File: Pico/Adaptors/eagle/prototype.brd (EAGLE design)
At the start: 45.8 x 20.7 mm, 13 parts, among them J1 JST-2P-SMD-PW-3410050P1

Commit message: minor board tweaks
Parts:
- flipped J1 to the bottom, turned to 90 degrees
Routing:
- net N$15: track 13.4 -> 20.2 mm
- net GND: track 20.2 -> 23.1 mm, vias 3 -> 2
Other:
- board text added: "Pico This Side"
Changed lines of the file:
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@@
 <wire x1="45.771" y1="20.437" x2="0" y2="20.564" width="0" layer="20"/>
 <wire x1="0" y1="20.564" x2="0" y2="0" width="0" layer="20"/>
+<text x="10.795" y="7.366" size="0.8128" layer="25">Pico This Side</text>
 </plain>
 <attributes>
@@
 <attribute name="VALUE" x="41.275" y="20.32" size="1.27" layer="27" rot="R270"/>
 </element>
-<element name="J1" library="OPL Eagle Library" package="2P-SMD-2.0-90D" value="JST-2P-SMD-PW-3410050P1" x="3.81" y="10.16" smashed="yes" rot="R270"/>
+<element name="J1" library="OPL Eagle Library" package="2P-SMD-2.0-90D" value="JST-2P-SMD-PW-3410050P1" x="3.81" y="10.16" smashed="yes" rot="MR90"/>
 </elements>
 <signals>
@@
 <contactref element="J1" pad="3"/>
 <contactref element="J1" pad="4"/>
-<wire x1="8.89" y1="9.16" x2="1.762" y2="9.16" width="0.6096" layer="1"/>
-<wire x1="1.762" y1="9.16" x2="1.651" y2="9.271" width="0.6096" layer="1"/>
-<wire x1="1.651" y1="9.271" x2="1.651" y2="14.038" width="0.6096" layer="1"/>
-<wire x1="1.651" y1="14.038" x2="1.629" y2="14.06" width="0.6096" layer="1"/>
-<wire x1="1.762" y1="9.16" x2="1.762" y2="6.393" width="0.6096" layer="1"/>
-<wire x1="1.762" y1="6.393" x2="1.629" y2="6.26" width="0.6096" layer="1"/>
-<wire x1="1.629" y1="6.26" x2="1.629" y2="4.169" width="0.6096" layer="1"/>
-<wire x1="1.629" y1="4.169" x2="1.27" y2="3.81" width="0.6096" layer="1"/>
-<via x="1.778" y="9.144" extent="1-16" drill="0.3048"/>
 <via x="19.558" y="14.224" extent="1-16" drill="0.3048"/>
 <via x="19.558" y="6.604" extent="1-16" drill="0.3048"/>
+<wire x1="1.27" y1="3.81" x2="1.27" y2="5.901" width="0.6096" layer="16"/>
+<wire x1="1.27" y1="5.901" x2="1.629" y2="6.26" width="0.6096" layer="16"/>
+<wire x1="1.629" y1="6.26" x2="1.629" y2="14.06" width="0.6096" layer="16"/>
+<wire x1="1.629" y1="14.06" x2="1.629" y2="11.198" width="0.6096" layer="16"/>
+<wire x1="1.629" y1="11.198" x2="1.651" y2="11.176" width="0.6096" layer="16"/>
+<wire x1="1.651" y1="11.176" x2="8.874" y2="11.176" width="0.6096" layer="16"/>
+<wire x1="8.874" y1="11.176" x2="8.89" y2="11.16" width="0.6096" layer="16"/>
 </signal>
 <signal name="N$9">
@@
 <wire x1="1.27" y1="16.51" x2="1.27" y2="19.05" width="1.016" layer="16"/>
 <contactref element="J1" pad="+"/>
-<wire x1="1.27" y1="16.51" x2="1.905" y2="16.51" width="0.6096" layer="1"/>
-<wire x1="1.905" y1="16.51" x2="4.064" y2="14.351" width="0.6096" layer="1"/>
-<wire x1="4.064" y1="14.351" x2="4.064" y2="12.573" width="0.6096" layer="1"/>
-<wire x1="4.064" y1="12.573" x2="5.461" y2="11.176" width="0.6096" layer="1"/>
-<wire x1="5.461" y1="11.176" x2="8.874" y2="11.176" width="0.6096" layer="1"/>
-<wire x1="8.874" y1="11.176" x2="8.89" y2="11.16" width="0.6096" layer="1"/>
+<wire x1="8.89" y1="9.16" x2="10.938" y2="9.16" width="0.6096" layer="16"/>
+<wire x1="10.938" y1="9.16" x2="11.811" y2="10.033" width="0.6096" layer="16"/>
+<wire x1="11.811" y1="10.033" x2="11.811" y2="11.938" width="0.6096" layer="16"/>
+<wire x1="11.811" y1="11.938" x2="10.795" y2="12.954" width="0.6096" layer="16"/>
+<wire x1="10.795" y1="12.954" x2="5.461" y2="12.954" width="0.6096" layer="16"/>
+<wire x1="5.461" y1="12.954" x2="2.159" y2="16.256" width="0.6096" layer="16"/>
+<wire x1="2.159" y1="16.256" x2="1.524" y2="16.256" width="0.6096" layer="16"/>
+<wire x1="1.524" y1="16.256" x2="1.27" y2="16.51" width="0.6096" layer="16"/>
 </signal>
 <signal name="N$16">

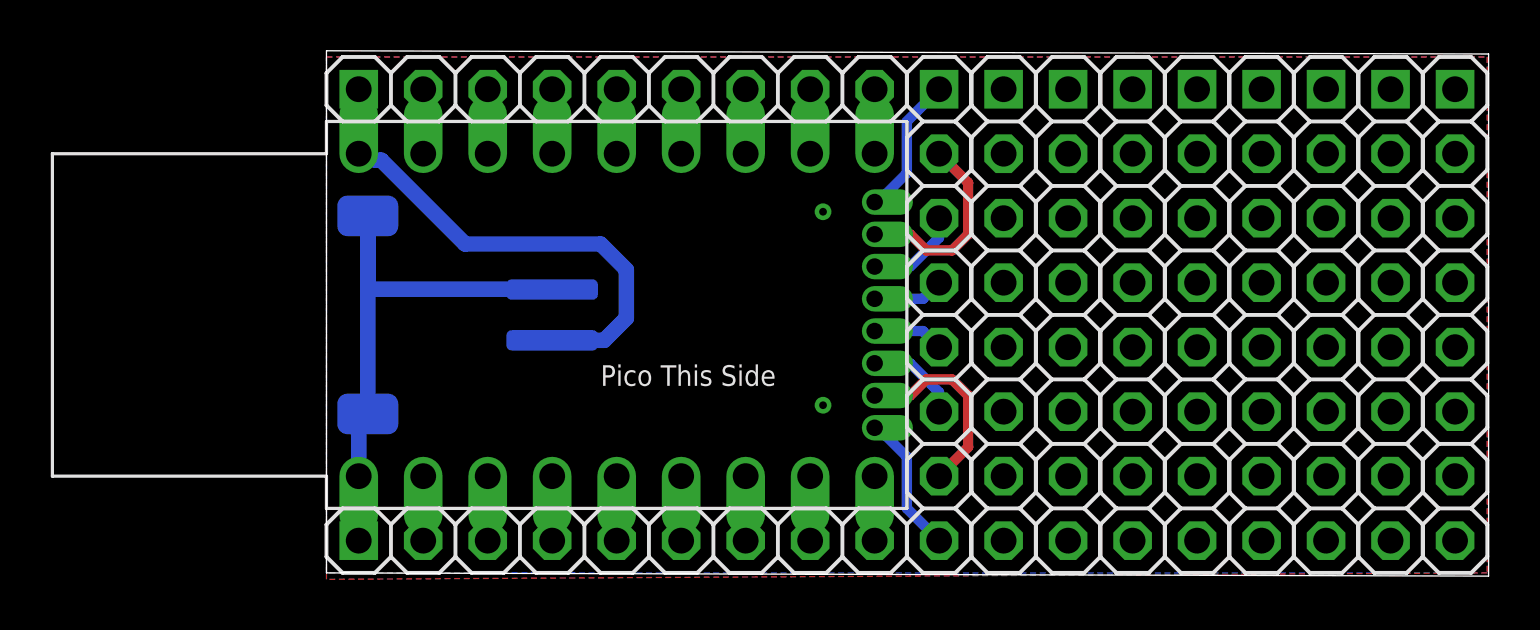
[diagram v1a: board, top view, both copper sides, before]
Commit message: Added battery charger pads to proto headers
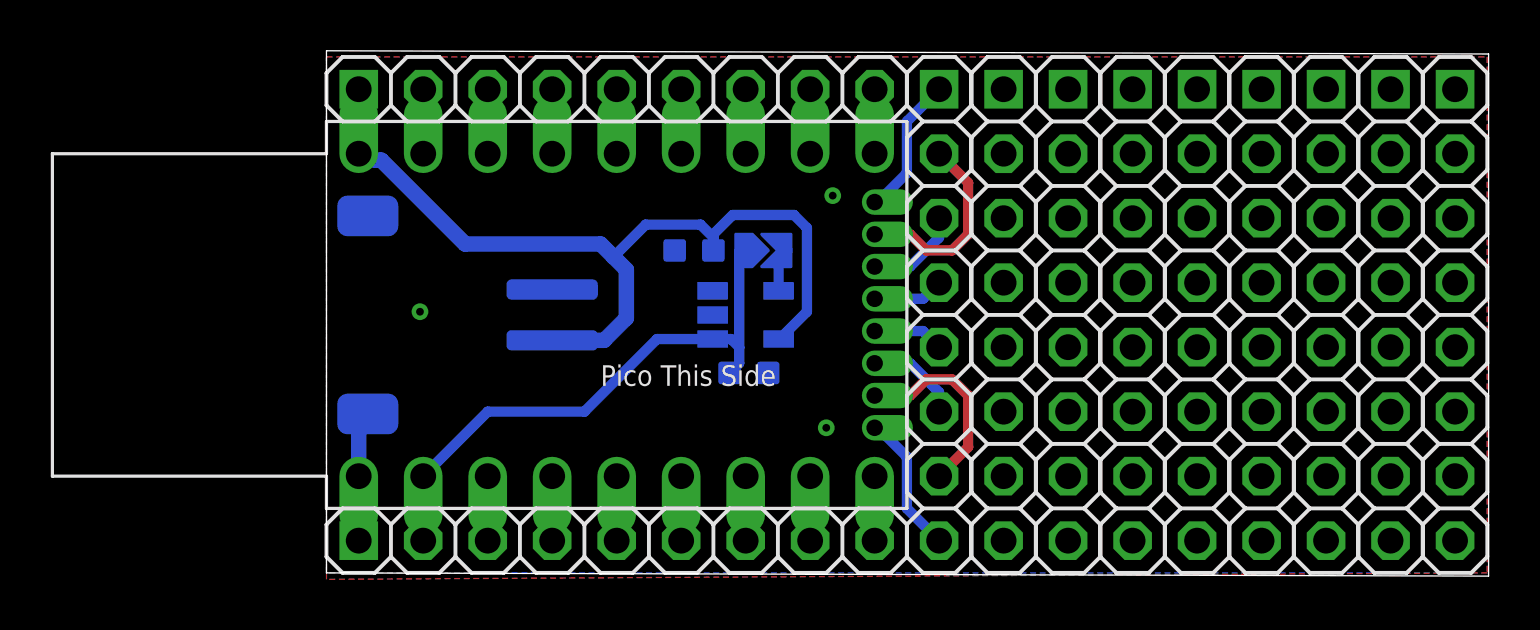
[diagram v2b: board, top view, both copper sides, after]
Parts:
- added C1, C2: 100nF, OPL5:C0603
- added U$4: SOLDERJUMPER, solder_jumper:SOLDERJUMPER
- added U3: MAX1551, template:SOT23-5
- J2: value JST-2P-SMD-PW-3410050P1 -> (none)
- renumbered J1 to J2
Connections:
- removed net 5V: JP4.2, U$1.5V
- removed net N$15: J2.+, JP3.1, U$1.BAT
- new net BAT: C1.1, J2.+, JP3.1, U$1.BAT, U3.5
- new net N$25: U$4.P$1, U3.4
- new net VIN: C2.1, JP4.2, U$1.5V, U$4.P$2, U3.1
- net GND: now also C1.2, C2.2, U3.2
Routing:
- net BAT: track 0.00 -> 35.0 mm
- net VIN: track 0.00 -> 22.3 mm
- net N$15: track 20.2 -> 0.00 mm
- net GND: track 23.1 -> 4.63 mm, vias 2 -> 3
- net 5V: track 2.54 -> 0.00 mm
- net N$25: track 0.00 -> 1.74 mm
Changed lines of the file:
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@@
 <layer number="111" name="111" color="7" fill="1" visible="no" active="no"/>
 <layer number="112" name="tSilk" color="7" fill="1" visible="no" active="no"/>
+<layer number="113" name="IDFDebug" color="7" fill="1" visible="yes" active="yes"/>
 <layer number="116" name="Patch_BOT" color="9" fill="4" visible="no" active="no"/>
 <layer number="118" name="Rect_Pads" color="7" fill="1" visible="no" active="no"/>
@@
 <layer number="223" name="223bmp" color="24" fill="1" visible="no" active="no"/>
 <layer number="224" name="224bmp" color="25" fill="1" visible="no" active="no"/>
+<layer number="225" name="225bmp" color="7" fill="1" visible="yes" active="yes"/>
+<layer number="226" name="226bmp" color="7" fill="1" visible="yes" active="yes"/>
+<layer number="227" name="227bmp" color="7" fill="1" visible="yes" active="yes"/>
+<layer number="228" name="228bmp" color="7" fill="1" visible="yes" active="yes"/>
+<layer number="230" name="230bmp" color="7" fill="1" visible="no" active="yes"/>
 <layer number="248" name="Housing" color="7" fill="1" visible="no" active="no"/>
 <layer number="249" name="Edge" color="7" fill="1" visible="no" active="no"/>
@@
 <classes>
 <class number="0" name="default" width="0.3048" drill="0">
+</class>
+<class number="1" name="power" width="0.4064" drill="0">
 </class>
 </classes>
@@
 <attribute name="VALUE" x="41.275" y="20.32" size="1.27" layer="27" rot="R270"/>
 </element>
-<element name="J1" library="OPL Eagle Library" package="2P-SMD-2.0-90D" value="JST-2P-SMD-PW-3410050P1" x="3.81" y="10.16" smashed="yes" rot="MR90"/>
+<element name="J2" library="OPL Eagle Library" package="2P-SMD-2.0-90D" value="" x="3.81" y="10.16" smashed="yes" rot="MR90">
+<attribute name="VALUE" x="3.81" y="8.255" size="0.635" layer="28" ratio="10" rot="MR90"/>
+</element>
+<element name="U3" library="template" package="SOT23-5" value="MAX1551" x="16.51" y="10.16" smashed="yes" rot="MR90">
+<attribute name="VALUE" x="18.7325" y="9.9695" size="0.635" layer="28" ratio="10" rot="MR90"/>
+</element>
+<element name="C2" library="OPL5" package="C0603" value="100nF" x="16.637" y="7.874" smashed="yes" rot="MR180">
+<attribute name="NAME" x="16.764" y="6.985" size="0.889" layer="26" ratio="11" rot="MR180"/>
+<attribute name="VALUE" x="14.097" y="6.7945" size="0.508" layer="28" ratio="10" rot="MR180"/>
+</element>
+<element name="C1" library="OPL5" package="C0603" value="100nF" x="14.478" y="12.7" smashed="yes" rot="MR0">
+<attribute name="NAME" x="16.383" y="13.716" size="0.889" layer="26" ratio="11" rot="MR0"/>
+<attribute name="VALUE" x="14.605" y="14.0335" size="0.508" layer="28" ratio="10" rot="MR0"/>
+</element>
+<element name="U$4" library="solder_jumper" package="SOLDERJUMPER" value="SOLDERJUMPER" x="17.399" y="12.7" rot="MR180"/>
 </elements>
 <signals>
@@
 <wire x1="25.273" y1="6.985" x2="25.273" y2="4.953" width="0.4064" layer="1"/>
 <wire x1="25.273" y1="4.953" x2="24.13" y2="3.81" width="0.4064" layer="1"/>
-</signal>
-<signal name="5V">
-<contactref element="U$1" pad="5V"/>
-<contactref element="JP4" pad="2"/>
-<wire x1="3.81" y1="3.81" x2="3.81" y2="1.27" width="1.016" layer="16"/>
 </signal>
 <signal name="GND">
@@
 <vertex x="0" y="0"/>
 </polygon>
-<contactref element="J1" pad="-"/>
-<contactref element="J1" pad="3"/>
-<contactref element="J1" pad="4"/>
-<via x="19.558" y="14.224" extent="1-16" drill="0.3048"/>
-<via x="19.558" y="6.604" extent="1-16" drill="0.3048"/>
+<via x="19.939" y="14.859" extent="1-16" drill="0.3048"/>
+<via x="19.685" y="5.715" extent="1-16" drill="0.3048"/>
 <wire x1="1.27" y1="3.81" x2="1.27" y2="5.901" width="0.6096" layer="16"/>
-<wire x1="1.27" y1="5.901" x2="1.629" y2="6.26" width="0.6096" layer="16"/>
-<wire x1="1.629" y1="6.26" x2="1.629" y2="14.06" width="0.6096" layer="16"/>
-<wire x1="1.629" y1="14.06" x2="1.629" y2="11.198" width="0.6096" layer="16"/>
-<wire x1="1.629" y1="11.198" x2="1.651" y2="11.176" width="0.6096" layer="16"/>
-<wire x1="1.651" y1="11.176" x2="8.874" y2="11.176" width="0.6096" layer="16"/>
-<wire x1="8.874" y1="11.176" x2="8.89" y2="11.16" width="0.6096" layer="16"/>
+<contactref element="U3" pad="2"/>
+<contactref element="C1" pad="2"/>
+<contactref element="C2" pad="2"/>
+<contactref element="J2" pad="-"/>
+<contactref element="J2" pad="3"/>
+<contactref element="J2" pad="4"/>
+<via x="3.683" y="10.287" extent="1-16" drill="0.3048"/>
 </signal>
 <signal name="N$9">
@@
 <wire x1="21.59" y1="3.81" x2="21.59" y2="1.27" width="1.016" layer="16"/>
 </signal>
-<signal name="N$15">
-<contactref element="U$1" pad="BAT"/>
-<contactref element="JP3" pad="1"/>
-<wire x1="1.27" y1="16.51" x2="1.27" y2="19.05" width="1.016" layer="16"/>
-<contactref element="J1" pad="+"/>
-<wire x1="8.89" y1="9.16" x2="10.938" y2="9.16" width="0.6096" layer="16"/>
-<wire x1="10.938" y1="9.16" x2="11.811" y2="10.033" width="0.6096" layer="16"/>
-<wire x1="11.811" y1="10.033" x2="11.811" y2="11.938" width="0.6096" layer="16"/>
-<wire x1="11.811" y1="11.938" x2="10.795" y2="12.954" width="0.6096" layer="16"/>
-<wire x1="10.795" y1="12.954" x2="5.461" y2="12.954" width="0.6096" layer="16"/>
-<wire x1="5.461" y1="12.954" x2="2.159" y2="16.256" width="0.6096" layer="16"/>
-<wire x1="2.159" y1="16.256" x2="1.524" y2="16.256" width="0.6096" layer="16"/>
-<wire x1="1.524" y1="16.256" x2="1.27" y2="16.51" width="0.6096" layer="16"/>
-</signal>
 <signal name="N$16">
 <contactref element="JP3" pad="2"/>
@@
 <wire x1="22.86" y1="17.78" x2="24.13" y2="19.05" width="0.4064" layer="16"/>
 </signal>
+<signal name="VIN" class="1">
+<contactref element="U3" pad="1"/>
+<contactref element="C2" pad="1"/>
+<contactref element="U$4" pad="P$2"/>
+<contactref element="U$1" pad="5V"/>
+<contactref element="JP4" pad="2"/>
+<wire x1="3.81" y1="3.81" x2="3.81" y2="1.27" width="1.016" layer="16"/>
+<wire x1="16.256" y1="12.7" x2="16.256" y2="8.89" width="0.4064" layer="16"/>
+<wire x1="16.256" y1="8.89" x2="16.256" y2="8.255" width="0.4064" layer="16"/>
+<wire x1="16.256" y1="8.255" x2="15.875" y2="7.874" width="0.4064" layer="16"/>
+<wire x1="15.2099" y1="9.21" x2="15.936" y2="9.21" width="0.4064" layer="16"/>
+<wire x1="15.936" y1="9.21" x2="16.256" y2="8.89" width="0.4064" layer="16"/>
+<wire x1="15.2099" y1="9.21" x2="13.02" y2="9.21" width="0.4064" layer="16"/>
+<wire x1="13.02" y1="9.21" x2="10.16" y2="6.35" width="0.4064" layer="16"/>
+<wire x1="10.16" y1="6.35" x2="6.35" y2="6.35" width="0.4064" layer="16"/>
+<wire x1="6.35" y1="6.35" x2="3.81" y2="3.81" width="0.4064" layer="16"/>
+</signal>
+<signal name="BAT">
+<contactref element="U3" pad="5"/>
+<contactref element="C1" pad="1"/>
+<contactref element="J2" pad="+"/>
+<contactref element="U$1" pad="BAT"/>
+<contactref element="JP3" pad="1"/>
+<wire x1="1.27" y1="16.51" x2="1.27" y2="19.05" width="1.016" layer="16"/>
+<wire x1="10.938" y1="9.16" x2="11.811" y2="10.033" width="0.6096" layer="16"/>
+<wire x1="11.811" y1="10.033" x2="11.811" y2="11.938" width="0.6096" layer="16"/>
+<wire x1="11.811" y1="11.938" x2="11.303" y2="12.446" width="0.6096" layer="16"/>
+<wire x1="11.303" y1="12.446" x2="10.795" y2="12.954" width="0.6096" layer="16"/>
+<wire x1="10.795" y1="12.954" x2="5.461" y2="12.954" width="0.6096" layer="16"/>
+<wire x1="5.461" y1="12.954" x2="2.159" y2="16.256" width="0.6096" layer="16"/>
+<wire x1="2.159" y1="16.256" x2="1.524" y2="16.256" width="0.6096" layer="16"/>
+<wire x1="1.524" y1="16.256" x2="1.27" y2="16.51" width="0.6096" layer="16"/>
+<wire x1="17.8101" y1="9.21" x2="17.846" y2="9.21" width="0.4064" layer="16"/>
+<wire x1="17.846" y1="9.21" x2="18.923" y2="10.287" width="0.4064" layer="16"/>
+<wire x1="18.923" y1="10.287" x2="18.923" y2="13.589" width="0.4064" layer="16"/>
+<wire x1="18.923" y1="13.589" x2="18.415" y2="14.097" width="0.4064" layer="16"/>
+<wire x1="18.415" y1="14.097" x2="16.002" y2="14.097" width="0.4064" layer="16"/>
+<wire x1="16.002" y1="14.097" x2="15.24" y2="13.335" width="0.4064" layer="16"/>
+<wire x1="15.24" y1="13.335" x2="15.24" y2="12.7" width="0.4064" layer="16"/>
+<wire x1="15.24" y1="12.7" x2="15.24" y2="13.208" width="0.4064" layer="16"/>
+<wire x1="15.24" y1="13.208" x2="14.732" y2="13.716" width="0.4064" layer="16"/>
+<wire x1="14.732" y1="13.716" x2="12.573" y2="13.716" width="0.4064" layer="16"/>
+<wire x1="12.573" y1="13.716" x2="11.303" y2="12.446" width="0.4064" layer="16"/>
+<wire x1="10.938" y1="9.16" x2="8.89" y2="9.16" width="0.6096" layer="16"/>
+</signal>
+<signal name="N$25">
+<contactref element="U3" pad="4"/>
+<contactref element="U$4" pad="P$1"/>
+<wire x1="17.8101" y1="11.11" x2="17.8101" y2="12.3491" width="0.4064" layer="16"/>
+<wire x1="17.8101" y1="12.3491" x2="18.161" y2="12.7" width="0.4064" layer="16"/>
+</signal>
 </signals>
